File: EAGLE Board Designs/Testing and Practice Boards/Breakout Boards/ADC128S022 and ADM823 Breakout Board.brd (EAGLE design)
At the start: 160 x 100 mm, 4 parts

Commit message: finish board
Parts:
- removed JP1, JP2: (no value), HyTechDevices:1X06
- added C1: 1uF, HyTechDevices:0603-CAP
- added C2: 0.1uF, HyTechDevices:0603-CAP
- added U$3: TEENSY_3.2_SIMPLE, HyTechDevices:TEENSY_3.2_SIMPLE
- moved U$2 93.0 mm to (22.0, 83.8)
- moved U$1 78.2 mm to (24.1, 69.8), turned to 90 degrees
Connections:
- net !MR!: now also U$3.A6; no longer JP2.5
- net !RESET!: now also U$3.A7; no longer JP2.6
- net +3V3: now also C1.1, C2.1, U$3.3.3V; no longer JP1.1
- net CS: now also U$3.D10(TX2); no longer JP1.4
- net GND: now also C1.2, C2.2, U$3.GND; no longer JP1.6
- net IN0: now also U$3.A1; no longer JP2.1
- net IN3: now also U$3.A2; no longer JP2.2
- net IN7: now also U$3.A0; no longer JP2.3
- net SCLK: now also U$3.D13; no longer JP1.2
- net SDI: now also U$3.D12; no longer JP1.3
- net SDO: now also U$3.D11; no longer JP1.5
- net WDI: now also U$3.A8; no longer JP2.4
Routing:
- net GND: track 0.00 -> 52.2 mm
- net +3V3: track 0.00 -> 40.6 mm
- net CS: track 0.00 -> 34.1 mm
- net SDI: track 0.00 -> 26.1 mm
- net SDO: track 0.00 -> 20.1 mm
- net IN0: track 0.00 -> 11.8 mm
- net IN3: track 0.00 -> 10.4 mm
- net WDI: track 0.00 -> 6.73 mm
- net IN7: track 0.00 -> 5.63 mm
- net SCLK: track 0.00 -> 4.59 mm
- net !RESET!: track 0.00 -> 2.97 mm
- net !MR!: track 0.00 -> 2.97 mm

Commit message: update schematic and board based on feedback
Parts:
- added C3: 0.1uF, HyTechDevices:0603-CAP
- added JP1, JP2: (no value), HyTechDevices:1X04
- added JP3: M02, HyTechDevices:1X02
- added R1: 1M, HyTechDevices:0603-RES
- added R2, R3: 10k, HyTechDevices:0603-RES
- moved U$3 20.4 mm to (21.6, 62.2), flipped to the bottom
- moved U$2 10.1 mm to (26.7, 92.7), flipped to the bottom
- moved U$1 8.52 mm to (27.9, 77.5), flipped to the bottom, turned to 180 degrees
- moved C1 7.96 mm to (25.5, 82.8), flipped to the bottom
- moved C2 7.90 mm to (23.5, 82.8), flipped to the bottom
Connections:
- new net +5V: C1.2, C2.2, U$1.2, U$3.VIN
- new net N$1: JP1.1, U$1.4
- new net N$2: JP1.2, U$1.5
- new net N$3: JP1.3, U$1.6
- new net N$4: JP1.4, U$1.7
- new net N$5: JP2.1, U$1.8
- new net N$6: JP2.2, U$1.9
- new net N$7: JP2.3, U$1.10
- new net N$8: JP2.4, U$1.11
- new net WATCHDOG_3V3: JP3.2, U$2.4
- new net WATCHDOG_GND: JP3.1, R1.1, R2.1, R3.2, U$2.2
- net !MR!: now also R1.2
- net !RESET!: now also R3.1
- net +3V3: now also C3.1; no longer C1.1, C2.1, U$1.2, U$2.4
- net GND: now also C1.1, C2.1, C3.2; no longer C1.2, C2.2, U$2.2
- net IN0: no longer U$1.4
- net IN3: no longer U$1.7
- net IN7: no longer U$1.11
- net WDI: now also R2.2
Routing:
- net +5V: track 0.00 -> 41.6 mm
- net +3V3: track 40.6 -> 78.4 mm
- net !MR!: track 2.97 -> 37.1 mm
- net !RESET!: track 2.97 -> 33.3 mm
- net WDI: track 6.73 -> 36.8 mm
- net SCLK: track 4.59 -> 26.5 mm
- net CS: track 34.1 -> 15.1 mm
- net WATCHDOG_GND: track 0.00 -> 17.7 mm
- net N$1: track 0.00 -> 15.4 mm
- net N$2: track 0.00 -> 14.6 mm
- net N$3: track 0.00 -> 13.6 mm
- net N$4: track 0.00 -> 13.2 mm
- net N$8: track 0.00 -> 12.8 mm
- net SDI: track 26.1 -> 13.8 mm
- net IN0: track 11.8 -> 0.00 mm
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- added copper zone on layer 16, net GND
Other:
- board size 160 x 100 mm -> 39.6 x 42 mm

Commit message: ready for manufacturing
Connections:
- removed net IN0: U$3.A1
- removed net IN3: U$3.A2
- removed net IN7: U$3.A0
- removed net WATCHDOG_GND: JP3.1, R1.1, R2.1, R3.2, U$2.2
- net !MR!: now also U$3.D2; no longer U$3.A6
- net !RESET!: now also U$3.D1(TX1); no longer U$3.A7
- net GND: now also JP3.1, R1.1, R2.1, R3.2, U$2.2
- net WDI: now also U$3.D0(RX1); no longer U$3.A8
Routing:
- net GND: track 59.6 -> 81.8 mm
- net !MR!: track 37.1 -> 18.7 mm
- net WDI: track 36.8 -> 18.6 mm
- net !RESET!: track 33.3 -> 15.5 mm
- net WATCHDOG_GND: track 17.7 -> 0.00 mm
- net +3V3: track 78.4 -> 64.4 mm
- net +5V: track 41.6 -> 28.7 mm
- net N$4: track 13.2 -> 10.8 mm
- net N$3: track 13.6 -> 11.6 mm
- net N$2: track 14.6 -> 12.8 mm
- net CS: track 15.1 -> 13.7 mm

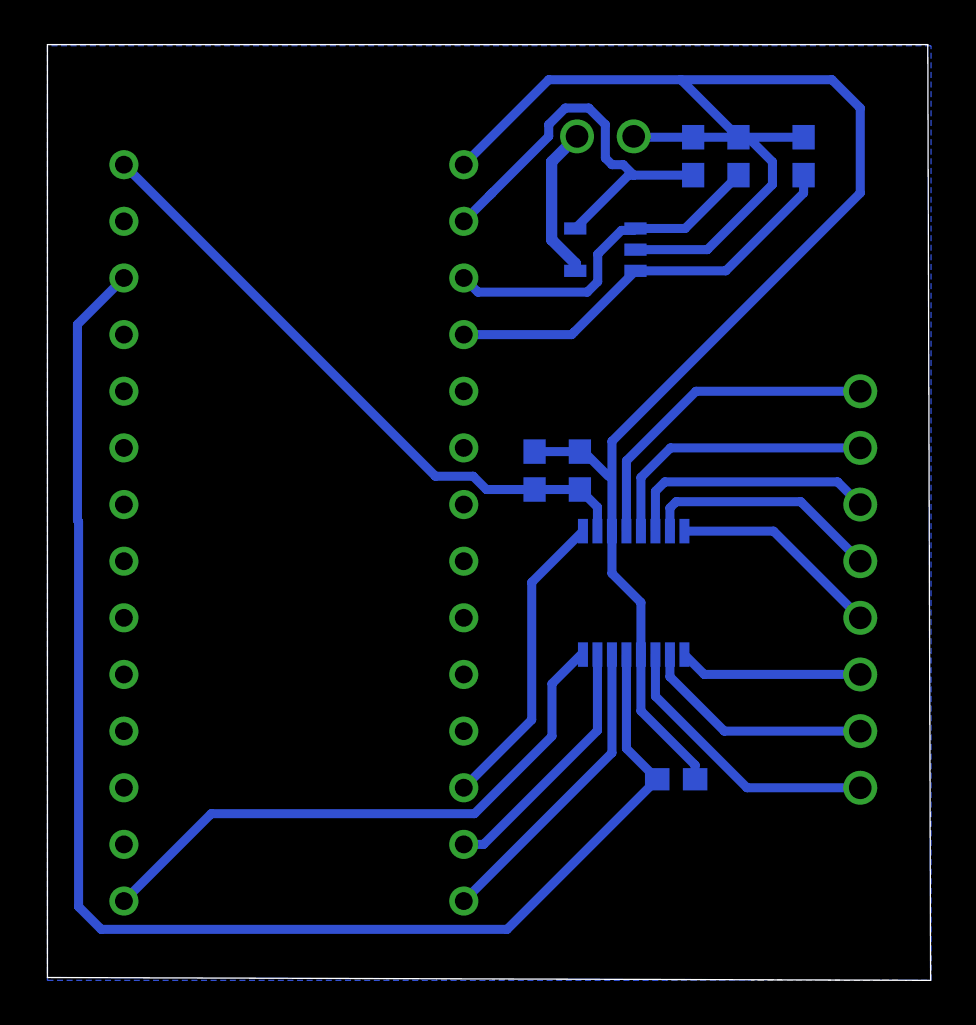
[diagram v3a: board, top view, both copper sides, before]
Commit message: fix watchdog package and pin issue
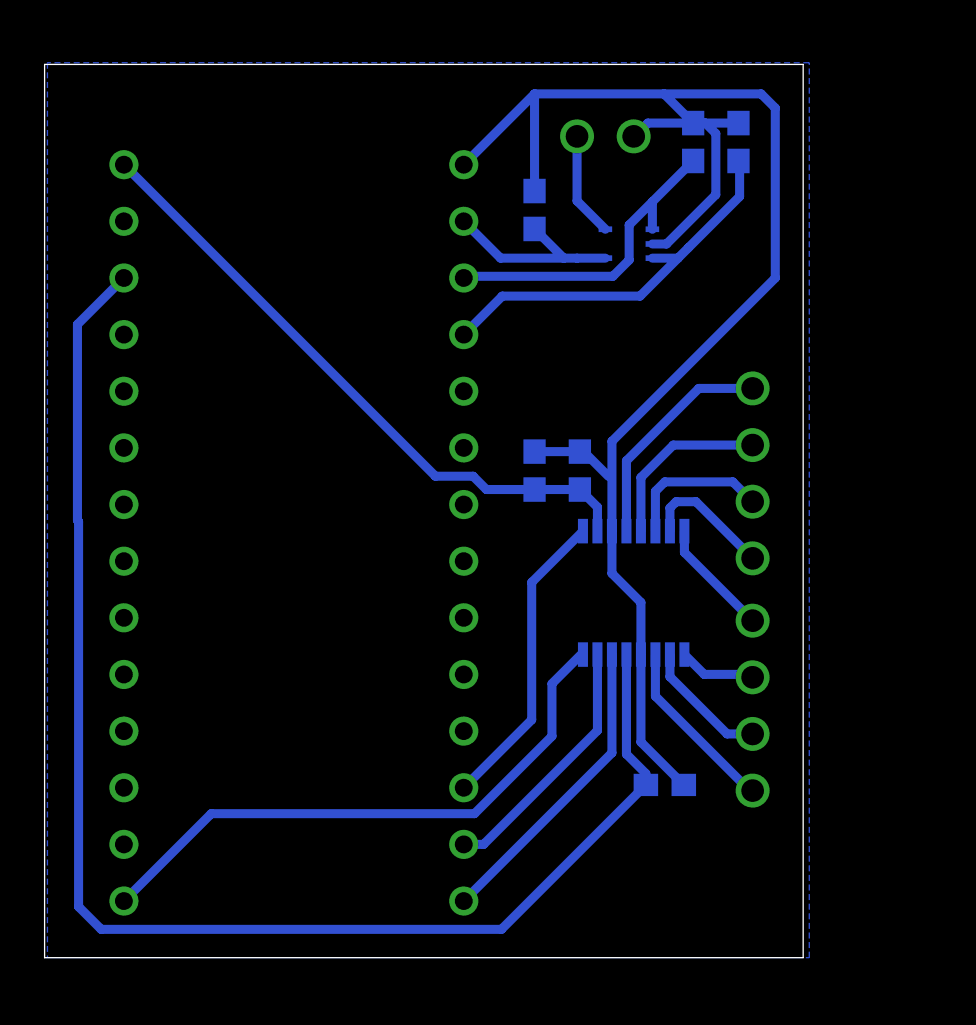
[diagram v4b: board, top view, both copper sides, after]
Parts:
- U$2: device HyTechDevices:SOT-23-5 -> HyTechDevices:SOT323-5
- moved R2 7.51 mm to (23.5, 94.5)
- moved JP1 4.83 mm to (33.3, 82.7)
- moved JP2 4.83 mm to (33.3, 72.3)
- moved R1 2.99 mm to (32.6, 97.5)
- moved R3 2.13 mm to (30.6, 97.5)
- moved C3 0.57 mm to (29.3, 68.7)
- moved U$2 0.38 mm to (26.7, 92.3)
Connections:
- net WATCHDOG_3V3: now also U$2.5; no longer U$2.4
- net WDI: now also U$2.4; no longer U$2.5
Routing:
- net WDI: track 18.6 -> 9.37 mm
- net GND: track 81.8 -> 73.2 mm
- net N$4: track 10.8 -> 5.92 mm
- net N$3: track 11.6 -> 6.69 mm
- net N$6: track 8.25 -> 3.48 mm
- net N$1: track 14.9 -> 10.2 mm
- net N$8: track 12.8 -> 7.98 mm
- net N$7: track 10.5 -> 5.77 mm
- net N$2: track 12.8 -> 8.02 mm
- net N$5: track 9.50 -> 5.28 mm
- net WATCHDOG_3V3: track 6.94 -> 4.69 mm
- net !MR!: track 18.7 -> 17.7 mm
- net !RESET!: track 15.5 -> 14.6 mm
- net +3V3: track 64.4 -> 63.8 mm
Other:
- board size 39.6 x 42 mm -> 34 x 40.1 mm

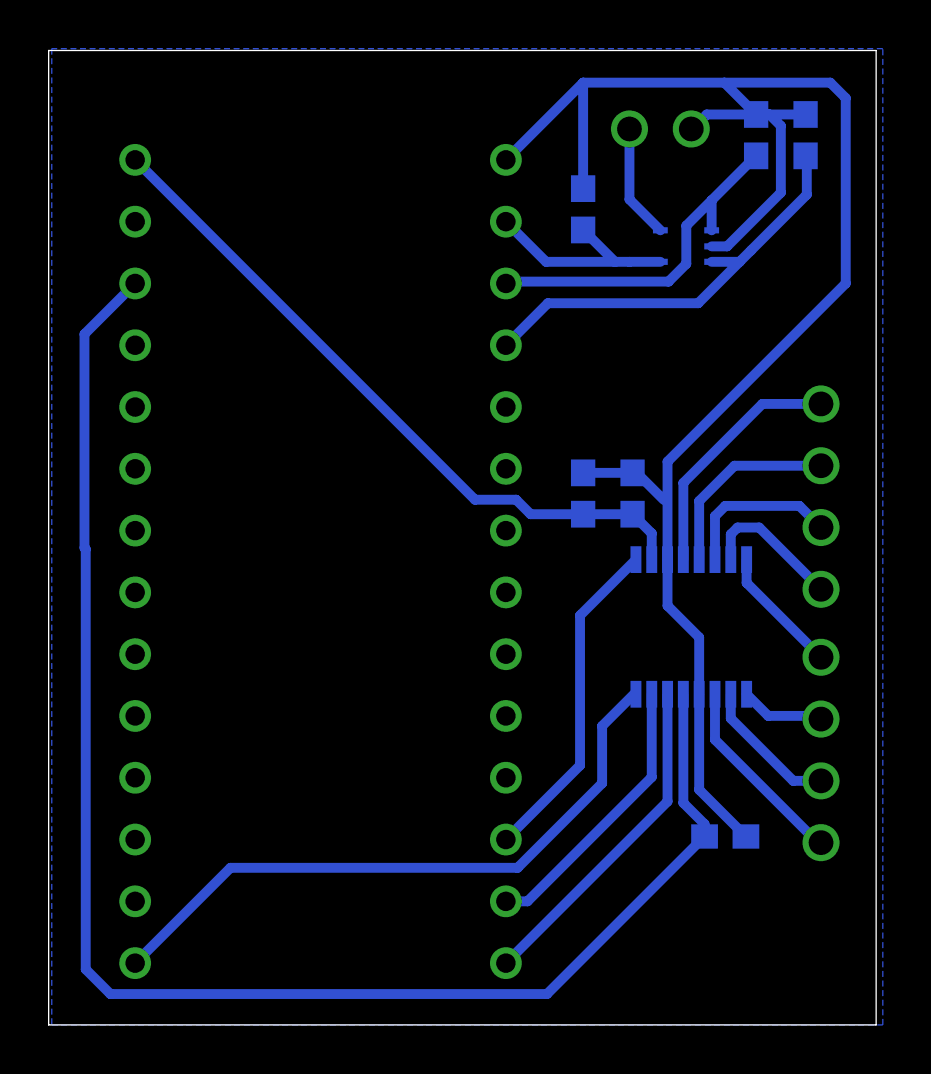
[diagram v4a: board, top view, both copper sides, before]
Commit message: update with correct drill sizes
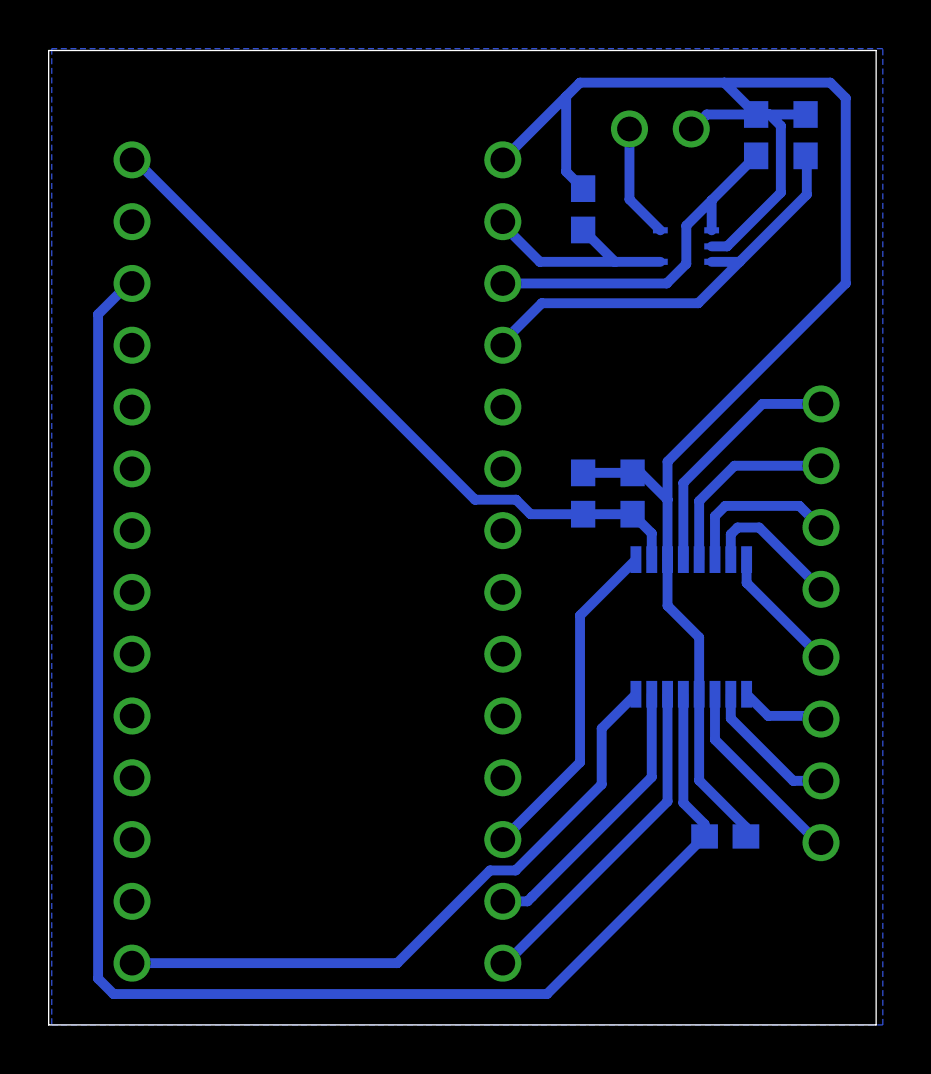
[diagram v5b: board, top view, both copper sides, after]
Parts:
- moved U$3 0.13 mm to (21.5, 62.2)
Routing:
- net +3V3: track 63.8 -> 63.3 mm
